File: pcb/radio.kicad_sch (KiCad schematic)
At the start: 6 parts, among them U4 SA868

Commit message: Merging in work from FSAE repo from when I forgot this one existed
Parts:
- removed U4: SA868, ev24-footprint-library:DRA818, symbol ev24:SA868
- added U4: SA868, 0_SA868:sa868, symbol 0_SA868:SA868
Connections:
- net +3V3: now also U4.8 (VCC)
- net AUDIO_IN: now also U4.18 (MIC_IN)
- net AUDIO_OUT: now also U4.3 (AF_OUT)
- net AUDIO_STATUS: now also U4.1 (~{Audio_ON})
- net GND: now also U4.10 (GND), U4.13 (NC), U4.14 (NC), U4.15 (NC), U4.2 (NC), U4.4 (NC), U4.9 (GND), U4.P1 (EP), U4.P2 (EP), U4.P3 (EP)
- net PTT: now also U4.5 (~{PTT})
- net RADIO_ON/OFF: now also U4.6 (PD)
- net UART_RX: now also U4.16 (RXD)
- net UART_TX: now also U4.17 (TXD)
- net at FL1.1 (IN): now also U4.12 (RF/ANT)
- net at R7.2: now also U4.7 (H/L)
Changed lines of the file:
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@@
+			"AAAAAAAAAAAAAAAAAAAAAAAAAAAAAAAAAAAAAAAAAAAAAAAAAAAAAAAAAAAAAAAAAAAAAAAAAAAA"
+			"AAAAAAAAAAAAAAAAAAAAAAAAAAAAAAAAAAAAAAAAAAAAAAAAAAAAAAAAAAAAAAAAAAAAAAAAAAAA"
+			"AAAAAAAAAAAAAAAAAAAAAAAAAAAAAAAAAAAAAAAAAAAAAIA/AAAAAAAAAAAAAIA/AAAAAAAAAAAA"
+			"AIA/AAAAAAAAAAAAAIA/AAAAAAAAAAAAAIA/AAAAAAAAAAAAAIA/AAAAAAAAAAAAAIA/AAAAAAAA"
+			"AAAAAIA/AAAAAAAAAAAAAIA/AAAAAAAAAAAAAIA/AAAAAAAAAAAAAIA/AAAAAAAAAAAAAIA/AAAA"
+			"AAAAAAAAAIA/AAAAAAAAAAAAAIA/AAAAAAAAAAAAAIA/AAAAAAAAAAAAAIA/AAAAAAAAAAAAAIA/"
+			"AAAAAAAAAAAAAIA/AAAAAAAAAAAAAIA/AAAAAAAAAAAAAIA/AAAAAAAAAAAAAIA/AAAAAAAAAAAA"
+			"AIA/AAAAAAAAAAAAAIA/AAAAAAAAAAAAAIA/AAAAAAAAAAAAAIA/AAAAAAAAAAAAAIA/AAAAAAAA"
+			"AAAAAIA/AAAAAAAAAAAAAIA/AAAAAAAAAAAAAIA/AAAAAAAAAAAAAIA/AAAAAAAAAAAAAIA/AAAA"
+			"AAAAAAAAAIA/AAAAAAAAAAAAAIA/AAAAAAAAAAAAAIA/AAAAAAAAAAAAAIA/AAAAAAAAAAAAAIA/"
+			"AAAAAAAAAAAAAIA/AAAAAAAAAAAAAIA/AAAAAAAAAAAAAIA/AAAAAAAAAABwJgAAAAAAANAEAAAA"
+			"AAAADvMFwEasxT5JgAo/IqYEwEasxT6scww/rBwGwEasxT41KSU/hbYIwEasxT5wQiE/DvMFwEas"
+			"xT5JgAo/rBwGwEasxT41KSU/rBwGwEasxT41KSU/mC8DwEasxT4hGg0/mC8DwEasxT4hdiY/mC8D"
+			"wEasxT4hdiY/mC8DwEasxT4hGg0/MbH5v0asxT4hdiY/mC8DwEasxT4hGg0/MbH5v0asxT4hGg0/"
+			"MbH5v0asxT4hdiY/IM0swEasxT7438o9IM0swEasxT4AAAAANV4WwEasxT7438o9IM0swEasxT4A"
+			"AAAANV4WwEasxT4AAAAANV4WwEasxT7438o9NV4WwEasxT4AAAAAv5oTwEasxT4hdqY7q+cUwEas"
+			"xT6pE9A9NV4WwEasxT7438o9NV4WwEasxT4AAAAAq+cUwEasxT6pE9A9v5oTwEasxT4hdqY7SdcQ"
+			"wEasxT4hdqY8v5oTwEasxT69rt89q+cUwEasxT6pE9A9v5oTwEasxT4hdqY7v5oTwEasxT69rt89"
+			"SdcQwEasxT4hdqY8DmcOwEasxT6D3TA9cXcSwEasxT4xsfk9v5oTwEasxT69rt89SdcQwEasxT4h"
+			"dqY8cXcSwEasxT4xsfk9cXcSwEasxT4xsfk9DmcOwEasxT6D3TA9IlQRwEasxT6scww+IlQRwEas"
+			"xT6scww+DmcOwEasxT6D3TA9rHMMwEasxQAAAAAAAAAAAAAAAAAAAAAAAAAAAAAAAAAAAAAAAAAA"
+			"AAAAAAAAAAAAAAAAAAAAAAAAAAAAAAAAAAAAAAAAAAAAAAAAAAAAAAAAAAAAAAAAAAAAAAAAAAAA"
+			"AAAAAAAAAAAAAAAAAAAAAAAAAAAAAAAAAAAAAAAAAAAAAAAAAAAAAAAAAAAAAAAAAAAAAAAAAAAA"
+			"AAAAAAAAAAAAAAAAAAAAAAAAAAAAAAAAAAAAAAAAAAAAAAAAAAAAAAAAAAAAAAAAAAAAAAAAAAAA"
+			"AAAAAAAAAAAAAAAAAAAAAAAAAAAAAAAAAAAAAAAAAAAAAAAAAAAAAAAAAAAAAAAAAAAAAAAAAAAA"
+			"AAAAAAAAAAAAAAAAAAAAAAAAAAAAAAAAAAAAAAAAAAAAAAAAAAAAAAAAAAAAAAAAAAAAAAAAAAAA"
+			"AAAAAAAAAAAAAAAAAAAAAAAAAAAAAAAAAAAAAAAAAAAAAAAAAAAAAAAAAAAAAAAAAAAAAAAAAAAA"
+			"AAAAAAAAAAAAAAAAAAAAAAAAAAAAAAAAAAAAAAAAAAAAAAAAAAAAAAAAAAAAAAAAAAAAAAAAAAAA"
+			"AAAAAAAAAAAAAAAAAAAAAAAAAAAAAAAAAAAAAAAAAAAAAAAAAAAAAAAAAAAAAAAAAAAAAAAAAAAA"
+			"AAAAAAAAAAAAAAAAAAAAAAAAAAAAAAAAAAAAAAAAAAAAAAAAAAAAAAAAAAAAAAAAAAAAAAAAAAAA"
+			"AAAAAAAAAAAAAAAAAAAAAAAAAAAAAAAAAAAAAAAAAAAAAAAAAAAAAAAAAAAAAAAAAAAAAAAAAAAA"
+			"AAAAAAAAAAAAAAAAAAAAAAAAAAAAAAAAAAAAAAAAAAAAAAAAAAAAAAAAAAAAAAAAAAAAAAAAAAAA"
+			"AAAAAAAAAAAAAAAAAAAAAAAAAAAAAAAAAAAAAAAAAAAAAAAAAAAAAAAAAAAAAAAAAAAAAAAAAAAA"
+			"AAAAAAAAAAAAAAAAAAAAAAAAAAAAAAAAAAAAAAAAAAAAAAAAAAAAAAAAAAAAAAAAAAAAAAAAAAAA"
+			"AAAAAAAAAAAAAAAAAAAAAAAAAAAAAAAAAAAAAAAAAAAAAAAAAAAAAAAAAAAAAAAAAAAAAAAAAAAA"
+			"AAAAAAAAAAAAAAAAAAAAAAAAAAAAAAAAAAAAAAAAAAAAAAAAAAAAAAAAAAAAAAAAAAAAAAAAAAAA"
 			"AAAAAAAAAAAAAAAAAAAAAAAAAAAAAAAAAAAAAAAAAAAAAAAAAAAAAAAAAAAAAAAAAAAAAAAAAAAA"
 			"AAAAAAAAAAAAAAAAAAAAAAAAAAAAAAAAAAAAAAAAAAAAAAAAAAAAAAAAAAAAAAAAAAAAAAAAAAAA"
@@
 	)
 	(symbol
-		(lib_id "ev24:SA868")
+		(lib_id "0_SA868:SA868")
 		(at 134.62 83.82 0)
 		(unit 1)
@@
 		(on_board yes)
 		(dnp no)
+		(fields_autoplaced yes)
 		(property "Reference" "U4"
-			(at 134.62 61.722 0)
+			(at 134.62 60.96 0)
 			(effects
 				(font
@@
 		)
 		(property "Value" "SA868"
-			(at 134.62 64.262 0)
-			(effects
-				(font
-					(size 1.27 1.27)
-				)
-			)
-		)
-		(property "Footprint" "ev24-footprint-library:DRA818"
+			(at 134.62 63.5 0)
+			(effects
+				(font
+					(size 1.27 1.27)
+				)
+			)
+		)
+		(property "Footprint" "0_SA868:sa868"
 			(at 132.08 81.28 0)
 			(effects
@@
 			)
 		)
+		(pin "P3"
+		)
+		(pin "12"
+		)
+		(pin "13"
+		)
+		(pin "10"
+		)
+		(pin "15"
+		)
+		(pin "17"
+		)
+		(pin "14"
+		)
+		(pin "2"
+		)
+		(pin "4"
+		)
+		(pin "11"
+		)
+		(pin "9"
+		)
+		(pin "P2"
+		)
+		(pin "8"
+		)
 		(pin "18"
 		)
+		(pin "6"
+		)
+		(pin "7"
+		)
+		(pin "3"
+		)
+		(pin "1"
+		)
+		(pin "P1"
+		)
 		(pin "16"
 		)
-		(pin "12"
-		)
-		(pin "10"
-		)
-		(pin "9"
-		)
 		(pin "5"
 		)
-		(pin "7"
-		)
-		(pin "3"
-		)
-		(pin "6"
-		)
-		(pin "8"
-		)
-		(pin "1"
-		)
-		(pin "17"
-		)
-		(pin "4"
-		)
-		(pin "2"
-		)
-		(pin "13"
-		)
-		(pin "15"
-		)
-		(pin "P3"
-		)
-		(pin "P1"
-		)
-		(pin "11"
-		)
-		(pin "14"
-		)
-		(pin "P2"
-		)
 		(instances
-			(project "driver-radio"
+			(project ""
 				(path "/1f94b0a1-b989-49dc-a3ab-12a0e728079d/63358803-d43b-4aec-8a20-c233ab97d197"
 					(reference "U4")

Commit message: Quite a few changes
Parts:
- added C6: 47u, Capacitor_SMD:C_1206_3216Metric, symbol Device:C
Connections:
- net +3V3: now also C6.1
- net GND: now also C6.2
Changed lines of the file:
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@@
+	)
+	(junction
+		(at 81.28 64.77)
+		(diameter 0)
+		(color 0 0 0 0)
 	)
 	(junction
@@
 	(wire
 		(pts
+			(xy 71.12 64.77) (xy 81.28 64.77)
+		)
+		(stroke
+			(width 0)
+			(type default)
+		)
+	)
+	(wire
+		(pts
 			(xy 151.13 91.44) (xy 157.48 91.44)
 		)
@@
 	(wire
 		(pts
+			(xy 71.12 67.31) (xy 71.12 64.77)
+		)
+		(stroke
+			(width 0)
+			(type default)
+		)
+	)
+	(wire
+		(pts
 			(xy 194.31 82.55) (xy 201.93 82.55)
 		)
@@
 	(wire
 		(pts
+			(xy 81.28 64.77) (xy 90.17 64.77)
+		)
+		(stroke
+			(width 0)
+			(type default)
+		)
+	)
+	(wire
+		(pts
 			(xy 104.14 64.77) (xy 110.49 64.77)
 		)
@@
 	(wire
 		(pts
+			(xy 71.12 76.2) (xy 81.28 76.2)
+		)
+		(stroke
+			(width 0)
+			(type default)
+		)
+	)
+	(wire
+		(pts
 			(xy 110.49 62.23) (xy 110.49 64.77)
 		)
@@
 	(wire
 		(pts
-			(xy 81.28 64.77) (xy 90.17 64.77)
-		)
-		(stroke
-			(width 0)
-			(type default)
-		)
-	)
-	(wire
-		(pts
 			(xy 115.57 92.71) (xy 118.11 92.71)
 		)
@@
 		(pts
 			(xy 162.56 82.55) (xy 173.99 82.55)
+		)
+		(stroke
+			(width 0)
+			(type default)
+		)
+	)
+	(wire
+		(pts
+			(xy 71.12 74.93) (xy 71.12 76.2)
 		)
 		(stroke
@@
 					(unit 1)
 				)
+			)
+		)
+	)
+	(symbol
+		(lib_id "Device:C")
+		(at 71.12 71.12 0)
+		(unit 1)
+		(exclude_from_sim no)
+		(in_bom yes)
+		(on_board yes)
+		(dnp no)
+		(property "Reference" "C6"
+			(at 63.754 69.596 0)
+			(effects
+				(font
+					(size 1.27 1.27)
+				)
+				(justify left)
+			)
+		)
+		(property "Value" "47u"
+			(at 64.262 72.136 0)
+			(effects
+				(font
+					(size 1.27 1.27)
+				)
+				(justify left)
+			)
+		)
+		(property "Footprint" "Capacitor_SMD:C_1206_3216Metric"
+			(at 72.0852 74.93 0)
+			(effects
+				(font
+					(size 1.27 1.27)
+				)
+				(hide yes)
+			)
+		)
+		(property "Datasheet" "~"
+			(at 71.12 71.12 0)
+			(effects
+				(font
+					(size 1.27 1.27)
+				)
+				(hide yes)
+			)
+		)
+		(property "Description" "Unpolarized capacitor"
+			(at 71.12 71.12 0)
+			(effects
+				(font
+					(size 1.27 1.27)
+				)
+				(hide yes)
+			)
+		)
+		(property "IPN" "CAP-000033-00"
+			(at 71.12 71.12 0)
+			(effects
+				(font
+					(size 1.27 1.27)
+				)
+				(hide yes)
+			)
+		)
+		(pin "2"
+		)
+		(pin "1"
+		)
+		(instances
+			(project "driver-radio"
+				(path "/1f94b0a1-b989-49dc-a3ab-12a0e728079d/63358803-d43b-4aec-8a20-c233ab97d197"
+					(reference "C6")
+					(unit 1)
+				)

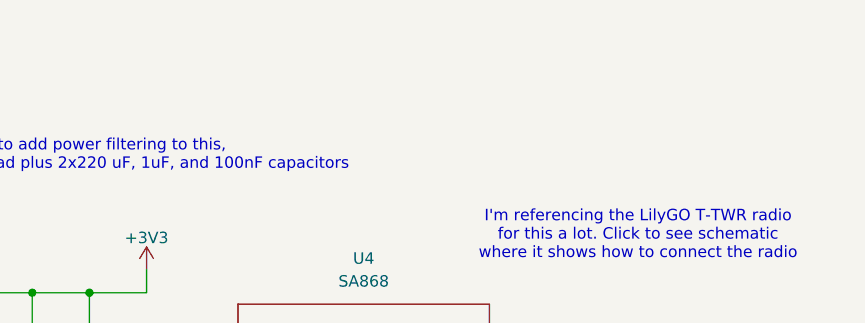
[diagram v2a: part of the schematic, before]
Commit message: updated footprints
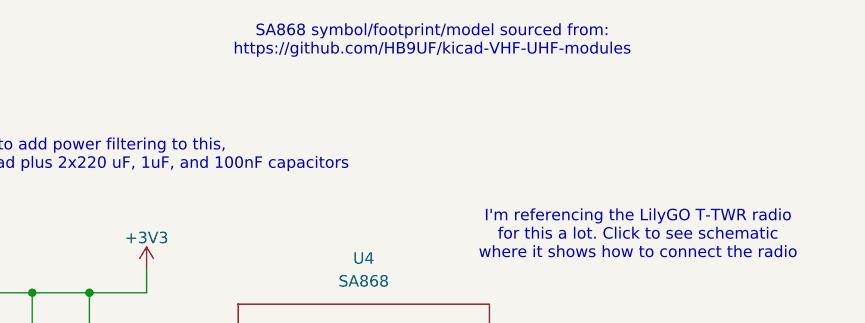
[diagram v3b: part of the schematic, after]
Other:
- note added: "SA868 symbol/footprint/model sourced from: https://github.com/HB9UF/kicad-VHF-UHF-modules"
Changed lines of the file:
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@@
+		)
+	)
+	(text "SA868 symbol/footprint/model sourced from:\nhttps://github.com/HB9UF/kicad-VHF-UHF-modules"
+		(exclude_from_sim no)
+		(at 142.24 36.83 0)
+		(effects
+			(font
+				(size 1.27 1.27)
+			)
+			(href "https://github.com/HB9UF/kicad-VHF-UHF-modules")
 		)
 	)
@@
 		(dnp no)
 		(fields_autoplaced yes)
-		(property "Reference" "FL1"
+		(property "Reference" "FL?"
 			(at 184.15 69.85 0)
 			(effects
@@
 				(path "/1f94b0a1-b989-49dc-a3ab-12a0e728079d/63358803-d43b-4aec-8a20-c233ab97d197"
 					(reference "FL1")
+					(unit 1)
+				)
+			)
+			(project "radio"
+				(path "/8aeca667-bfe2-4ef6-9722-308d4d299873"
+					(reference "FL?")
 					(unit 1)
 				)
@@
 		(dnp no)
 		(fields_autoplaced yes)
-		(property "Reference" "#PWR021"
+		(property "Reference" "#PWR?"
 			(at 81.28 83.82 0)
 			(effects
@@
 				(path "/1f94b0a1-b989-49dc-a3ab-12a0e728079d/63358803-d43b-4aec-8a20-c233ab97d197"
 					(reference "#PWR021")
+					(unit 1)
+				)
+			)
+			(project "radio"
+				(path "/8aeca667-bfe2-4ef6-9722-308d4d299873"
+					(reference "#PWR?")
 					(unit 1)
 				)
@@
 		(on_board yes)
 		(dnp no)
-		(property "Reference" "C6"
+		(property "Reference" "C?"
 			(at 63.754 69.596 0)
 			(effects
@@
 				(path "/1f94b0a1-b989-49dc-a3ab-12a0e728079d/63358803-d43b-4aec-8a20-c233ab97d197"
 					(reference "C6")
+					(unit 1)
+				)
+			)
+			(project "radio"
+				(path "/8aeca667-bfe2-4ef6-9722-308d4d299873"
+					(reference "C?")
 					(unit 1)
 				)
@@
 		(dnp no)
 		(fields_autoplaced yes)
-		(property "Reference" "#PWR022"
+		(property "Reference" "#PWR?"
 			(at 90.17 115.57 0)
 			(effects
@@
 				(path "/1f94b0a1-b989-49dc-a3ab-12a0e728079d/63358803-d43b-4aec-8a20-c233ab97d197"
 					(reference "#PWR022")
+					(unit 1)
+				)
+			)
+			(project "radio"
+				(path "/8aeca667-bfe2-4ef6-9722-308d4d299873"
+					(reference "#PWR?")
 					(unit 1)
 				)
@@
 		(on_board yes)
 		(dnp no)
-		(property "Reference" "C15"
+		(property "Reference" "C?"
 			(at 92.456 69.596 0)
 			(effects
@@
 				(path "/1f94b0a1-b989-49dc-a3ab-12a0e728079d/63358803-d43b-4aec-8a20-c233ab97d197"
 					(reference "C15")
+					(unit 1)
+				)
+			)
+			(project "radio"
+				(path "/8aeca667-bfe2-4ef6-9722-308d4d299873"
+					(reference "C?")
 					(unit 1)
 				)
@@
 		(dnp no)
 		(fields_autoplaced yes)
-		(property "Reference" "#PWR031"
+		(property "Reference" "#PWR?"
 			(at 134.62 121.92 0)
 			(effects
@@
 				(path "/1f94b0a1-b989-49dc-a3ab-12a0e728079d/63358803-d43b-4aec-8a20-c233ab97d197"
 					(reference "#PWR031")
+					(unit 1)
+				)
+			)
+			(project "radio"
+				(path "/8aeca667-bfe2-4ef6-9722-308d4d299873"
+					(reference "#PWR?")
 					(unit 1)
 				)
@@
 		(on_board yes)
 		(dnp no)
-		(property "Reference" "#PWR025"
+		(property "Reference" "#PWR?"
 			(at 110.49 66.04 0)
 			(effects
@@
 				(path "/1f94b0a1-b989-49dc-a3ab-12a0e728079d/63358803-d43b-4aec-8a20-c233ab97d197"
 					(reference "#PWR025")
+					(unit 1)
+				)
+			)
+			(project "radio"
+				(path "/8aeca667-bfe2-4ef6-9722-308d4d299873"
+					(reference "#PWR?")
 					(unit 1)
 				)
@@
 		(on_board yes)
 		(dnp no)
-		(property "Reference" "C14"
+		(property "Reference" "C?"
 			(at 83.566 69.596 0)
 			(effects
@@
 				(path "/1f94b0a1-b989-49dc-a3ab-12a0e728079d/63358803-d43b-4aec-8a20-c233ab97d197"
 					(reference "C14")
+					(unit 1)
+				)
+			)
+			(project "radio"
+				(path "/8aeca667-bfe2-4ef6-9722-308d4d299873"
+					(reference "C?")
 					(unit 1)
 				)
@@
 		(on_board yes)
 		(dnp no)
-		(property "Reference" "#PWR035"
+		(property "Reference" "#PWR?"
 			(at 184.15 102.87 0)
 			(effects
@@
 				(path "/1f94b0a1-b989-49dc-a3ab-12a0e728079d/63358803-d43b-4aec-8a20-c233ab97d197"
 					(reference "#PWR035")
+					(unit 1)
+				)
+			)
+			(project "radio"
+				(path "/8aeca667-bfe2-4ef6-9722-308d4d299873"
+					(reference "#PWR?")
 					(unit 1)
 				)
@@
 		(on_board yes)
 		(dnp yes)
-		(property "Reference" "R7"
+		(property "Reference" "R?"
 			(at 92.202 104.1399 0)
 			(effects
@@
 				(path "/1f94b0a1-b989-49dc-a3ab-12a0e728079d/63358803-d43b-4aec-8a20-c233ab97d197"
 					(reference "R7")
+					(unit 1)
+				)
+			)
+			(project "radio"
+				(path "/8aeca667-bfe2-4ef6-9722-308d4d299873"
+					(reference "R?")
 					(unit 1)
 				)
@@
 		(on_board yes)
 		(dnp no)
-		(property "Reference" "C13"
+		(property "Reference" "C?"
 			(at 73.914 69.596 0)
 			(effects
@@
 				(path "/1f94b0a1-b989-49dc-a3ab-12a0e728079d/63358803-d43b-4aec-8a20-c233ab97d197"
 					(reference "C13")
+					(unit 1)
+				)
+			)
+			(project "radio"
+				(path "/8aeca667-bfe2-4ef6-9722-308d4d299873"
+					(reference "C?")
 					(unit 1)
 				)
@@
 		(dnp no)
 		(fields_autoplaced yes)
-		(property "Reference" "U4"
+		(property "Reference" "U?"
 			(at 134.62 60.96 0)
 			(effects
@@
 				)
 			)
-		)
-	)
+			(project "radio"
+				(path "/8aeca667-bfe2-4ef6-9722-308d4d299873"
+					(reference "U?")
+					(unit 1)
+				)
+			)
+		)
+	)
+	(sheet_instances
+		(path "/"
+			(page "1")
+		)
+	)
+	(embedded_fonts no)
 )

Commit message: added 3d model
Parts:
- U4: footprint 0_SA868:sa868 -> VHF_UHF_Modules:VHF_UHF_Module_generic
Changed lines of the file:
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@@
 		(dnp no)
 		(fields_autoplaced yes)
-		(property "Reference" "FL?"
+		(property "Reference" "FL1"
 			(at 184.15 69.85 0)
 			(effects
@@
 		(dnp no)
 		(fields_autoplaced yes)
-		(property "Reference" "#PWR?"
+		(property "Reference" "#PWR021"
 			(at 81.28 83.82 0)
 			(effects
@@
 		(on_board yes)
 		(dnp no)
-		(property "Reference" "C?"
+		(property "Reference" "C6"
 			(at 63.754 69.596 0)
 			(effects
@@
 		(dnp no)
 		(fields_autoplaced yes)
-		(property "Reference" "#PWR?"
+		(property "Reference" "#PWR022"
 			(at 90.17 115.57 0)
 			(effects
@@
 		(on_board yes)
 		(dnp no)
-		(property "Reference" "C?"
+		(property "Reference" "C15"
 			(at 92.456 69.596 0)
 			(effects
@@
 		(dnp no)
 		(fields_autoplaced yes)
-		(property "Reference" "#PWR?"
+		(property "Reference" "#PWR031"
 			(at 134.62 121.92 0)
 			(effects
@@
 		(on_board yes)
 		(dnp no)
-		(property "Reference" "#PWR?"
+		(property "Reference" "#PWR025"
 			(at 110.49 66.04 0)
 			(effects
@@
 		(on_board yes)
 		(dnp no)
-		(property "Reference" "C?"
+		(property "Reference" "C14"
 			(at 83.566 69.596 0)
 			(effects
@@
 		(on_board yes)
 		(dnp no)
-		(property "Reference" "#PWR?"
+		(property "Reference" "#PWR035"
 			(at 184.15 102.87 0)
 			(effects
@@
 		(on_board yes)
 		(dnp yes)
-		(property "Reference" "R?"
+		(property "Reference" "R7"
 			(at 92.202 104.1399 0)
 			(effects
@@
 		(on_board yes)
 		(dnp no)
-		(property "Reference" "C?"
+		(property "Reference" "C13"
 			(at 73.914 69.596 0)
 			(effects
@@
 		(dnp no)
 		(fields_autoplaced yes)
-		(property "Reference" "U?"
+		(property "Reference" "U4"
 			(at 134.62 60.96 0)
 			(effects
@@
 			)
 		)
-		(property "Footprint" "0_SA868:sa868"
+		(property "Footprint" "VHF_UHF_Modules:VHF_UHF_Module_generic"
 			(at 132.08 81.28 0)
 			(effects
